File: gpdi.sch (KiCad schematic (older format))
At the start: 20 parts, among them U1 LFE5U-45F-6BG381C, U11 PCA9306D

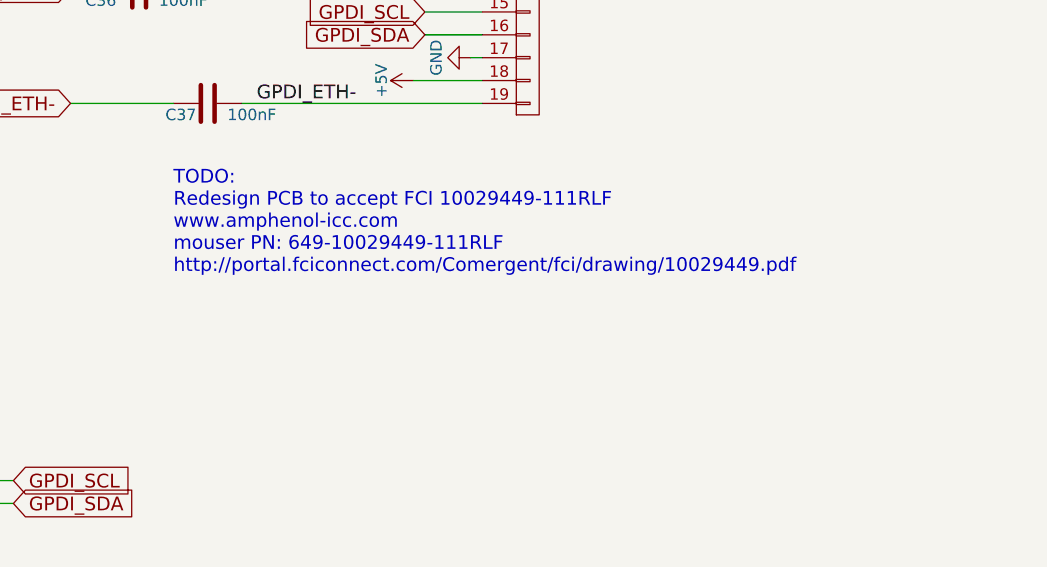
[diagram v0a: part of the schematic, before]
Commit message: schematics: GPDI1 connector part number set to FCI 10029449-111RLF
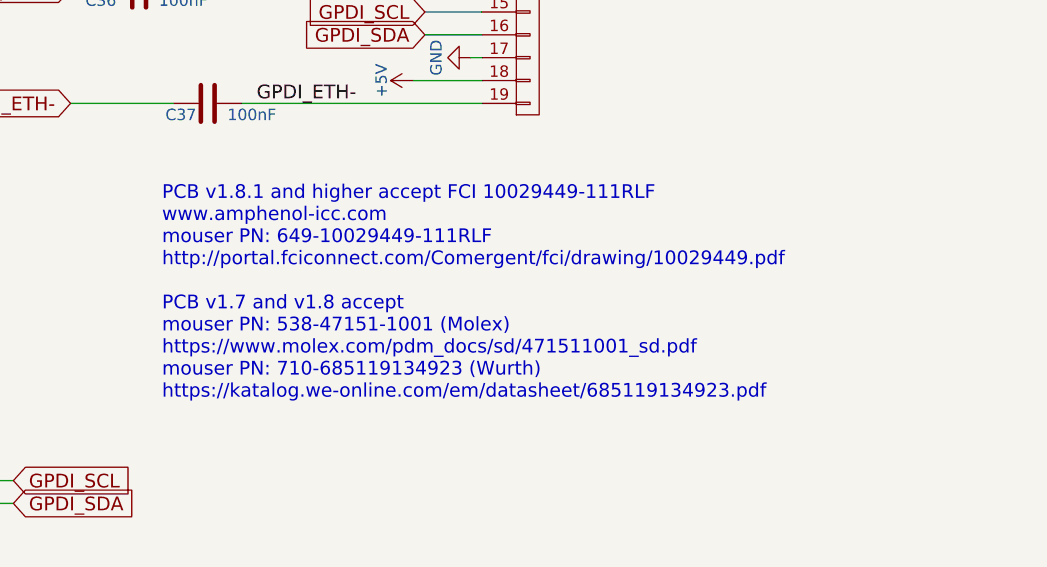
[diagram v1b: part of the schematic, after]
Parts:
- GPDI1: Distributor1_PN 710-685119134923 -> 649-10029449-111RLF; Distributor2_PN: 538-47151-1001 -> (none); Distributor2_URL www.mouser.com -> (none); MFG2_PN 47151-1001 -> (none); MFG2_URL www.molex.com -> (none); MFG_PN 685119134923 -> 10029449-111RLF; MFG_URL www.we-online.com -> www.amphenol-icc.com
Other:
- note added: "PCB v1.8.1 and higher accept FCI 10029449-111RLF\nwww.amphenol-icc.com\nmouser PN: 649-10029449-111RLF\nhttp://portal.fciconnect.com/Comergent/fci/drawing/10029449.pdf\n\nPCB v1.7 and v1.8 accept\nmouser PN: 538-47151-1001 (Molex)\nhttps://www.molex.com/pdm_docs/sd/471511001_sd.pdf\nmouser PN: 710-685119134923 (Wurth)\nhttps://katalog.we-online.com/em/datasheet/685119134923.pdf"
- note removed: "TODO:\nRedesign PCB to accept FCI 10029449-111RLF\nwww.amphenol-icc.com\nmouser PN: 649-10029449-111RLF\nhttp://portal.fciconnect.com/Comergent/fci/drawing/10029449.pdf\n"
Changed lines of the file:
@@
 F 1 "GPDI-D" V 9050 2950 50  0000 C CNN
 F 2 "conn-fci:CONN-10029449-111RLF" H 8950 2950 60  0001 C CNN
-F 3 "https://katalog.we-online.com/em/datasheet/685119134923.pdf" H 8950 2950 60  0001 C CNN
-F 4 "www.we-online.com" H 8950 2950 60  0001 C CNN "MFG_URL"
-F 5 "685119134923" H 8950 2950 60  0001 C CNN "MFG_PN"
-F 6 "www.molex.com" H 8950 2950 50  0001 C CNN "MFG2_URL"
-F 7 "47151-1001" H 8950 2950 50  0001 C CNN "MFG2_PN"
-F 8 "www.mouser.com" H 8950 2950 60  0001 C CNN "Distributor1_URL"
-F 9 "710-685119134923" H 8950 2950 60  0001 C CNN "Distributor1_PN"
-F 10 "www.mouser.com" H 8950 2950 50  0001 C CNN "Distributor2_URL"
-F 11 "538-47151-1001" H 8950 2950 50  0001 C CNN "Distributor2_PN:"
+F 3 "http://portal.fciconnect.com/Comergent/fci/drawing/10029449.pdf" H 8950 2950 60  0001 C CNN
+F 4 "www.amphenol-icc.com" H 8950 2950 60  0001 C CNN "MFG_URL"
+F 5 "10029449-111RLF" H 8950 2950 60  0001 C CNN "MFG_PN"
+F 6 "www.mouser.com" H 8950 2950 60  0001 C CNN "Distributor1_URL"
+F 7 "649-10029449-111RLF" H 8950 2950 60  0001 C CNN "Distributor1_PN"
 	1    8950 2950
 	1    0    0    -1
@@
 Wire Wire Line
 	6100 5450 6100 5750
-Text Notes 7400 4650 0    60   ~ 0
-TODO:\nRedesign PCB to accept FCI 10029449-111RLF\nwww.amphenol-icc.com\nmouser PN: 649-10029449-111RLF\nhttp://portal.fciconnect.com/Comergent/fci/drawing/10029449.pdf\n
+Text Notes 7350 5200 0    60   ~ 0
+PCB v1.8.1 and higher accept FCI 10029449-111RLF\nwww.amphenol-icc.com\nmouser PN: 649-10029449-111RLF\nhttp://portal.fciconnect.com/Comergent/fci/drawing/10029449.pdf\n\nPCB v1.7 and v1.8 accept\nmouser PN: 538-47151-1001 (Molex)\nhttps://www.molex.com/pdm_docs/sd/471511001_sd.pdf\nmouser PN: 710-685119134923 (Wurth)\nhttps://katalog.we-online.com/em/datasheet/685119134923.pdf
 $EndSCHEMATC

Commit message: schematics: replace 45F chip with 85F
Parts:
- U1: value LFE5U-45F-6BG381C -> LFE5U-85F-6BG381C; symbol lfe5bg381:LFE5U-45F-6BG381C -> lfe5bg381:LFE5U-85F-6BG381C; MFG_PN LFE5U-45F-6BG381C -> LFE5U-85F-6BG381C
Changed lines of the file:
@@
 	6100 4850 6300 4850
 $Comp
-L lfe5bg381:LFE5U-45F-6BG381C U1
+L lfe5bg381:LFE5U-85F-6BG381C U1
 U 2 1 5A07A906
 P 3600 2900
@@
 AR Path="/58D686D9/5A07A906" Ref="U1"  Part="2"
 F 0 "U1" H 3600 3850 60  0000 C CNN
-F 1 "LFE5U-45F-6BG381C" H 3600 3750 60  0000 C CNN
+F 1 "LFE5U-85F-6BG381C" H 3600 3750 60  0000 C CNN
 F 2 "lfe5bg381:BGA-381_pitch0.8mm_dia0.4mm" H 2550 3850 60  0001 C CNN
 F 3 "http://www.latticesemi.com/~/media/LatticeSemi/Documents/DataSheets/ECP5/FPGA-DS-02012.pdf" H 2550 3850 60  0001 C CNN
-F 4 "LFE5U-45F-6BG381C" H 3600 2900 60  0001 C CNN "MFG_PN"
+F 4 "LFE5U-85F-6BG381C" H 3600 2900 60  0001 C CNN "MFG_PN"
 F 5 "www.mouser.com" H 3600 2900 60  0001 C CNN "Distributor1_URL"
 	2    3600 2900

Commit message: schematics: instead of micro-gpdi-d symbol using gpdi-d
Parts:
- GPDI1: symbol micro-hdmi-d:MICRO-HDMI-D -> hdmi-d:HDMI-D
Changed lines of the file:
@@
 $EndDescr
 $Comp
-L micro-hdmi-d:MICRO-HDMI-D GPDI1
+L hdmi-d:HDMI-D GPDI1
 U 1 1 58D69067
 P 8950 2950

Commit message: schematics: hopefully getting rid of all references to micro-gpdi-d
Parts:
- U11: symbol micro-hdmi-d:DIL8 -> Connector_Generic:Conn_02x04_Counter_Clockwise
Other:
- moved on the sheet: R22, R23
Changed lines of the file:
@@
 GPDI_SDA
 $Comp
-L micro-hdmi-d:DIL8 U11
+L Connector_Generic:Conn_02x04_Counter_Clockwise U11
 U 1 1 58D91A1E
-P 5300 5500
-F 0 "U11" H 5300 5750 50  0000 C CNN
-F 1 "PCA9306D" H 5300 5250 50  0000 C CNN
-F 2 "SM8:SM8" H 5300 5500 50  0001 C CNN
-F 3 "https://www.nxp.com/docs/en/data-sheet/PCA9306.pdf" H 5300 5500 50  0001 C CNN
-F 4 "www.nxp.com" H 5300 5500 60  0001 C CNN "MFG_URL"
-F 5 "PCA9306D" H 5300 5500 60  0001 C CNN "MFG_PN"
-F 6 "www.mouser.com" H 5300 5500 60  0001 C CNN "Distributor1_URL"
-F 7 "771-PCA9306D-T" H 5300 5500 60  0001 C CNN "Distributor1_PN"
-	1    5300 5500
+P 5350 5450
+F 0 "U11" H 5400 5650 50  0000 C CNN
+F 1 "PCA9306D" H 5400 5150 50  0000 C CNN
+F 2 "SM8:SM8" H 5350 5450 50  0001 C CNN
+F 3 "https://www.nxp.com/docs/en/data-sheet/PCA9306.pdf" H 5350 5450 50  0001 C CNN
+F 4 "www.nxp.com" H 5350 5450 60  0001 C CNN "MFG_URL"
+F 5 "PCA9306D" H 5350 5450 60  0001 C CNN "MFG_PN"
+F 6 "www.mouser.com" H 5350 5450 60  0001 C CNN "Distributor1_URL"
+F 7 "771-PCA9306D-T" H 5350 5450 60  0001 C CNN "Distributor1_PN"
+	1    5350 5450
 	1    0    0    -1
 $EndComp
@@
 L power:+3V3 #PWR091
 U 1 1 58D92A40
-P 4700 5000
-F 0 "#PWR091" H 4700 4850 50  0001 C CNN
-F 1 "+3V3" H 4700 5140 50  0000 C CNN
-F 2 "" H 4700 5000 50  0000 C CNN
-F 3 "" H 4700 5000 50  0000 C CNN
-	1    4700 5000
+P 4900 5000
+F 0 "#PWR091" H 4900 4850 50  0001 C CNN
+F 1 "+3V3" H 4900 5140 50  0000 C CNN
+F 2 "" H 4900 5000 50  0000 C CNN
+F 3 "" H 4900 5000 50  0000 C CNN
+	1    4900 5000
 	1    0    0    -1
 $EndComp
@@
 L power:GND #PWR092
 U 1 1 58D92B02
-P 4950 5350
-F 0 "#PWR092" H 4950 5100 50  0001 C CNN
-F 1 "GND" H 4950 5200 50  0000 C CNN
-F 2 "" H 4950 5350 50  0000 C CNN
-F 3 "" H 4950 5350 50  0000 C CNN
-	1    4950 5350
+P 5150 5350
+F 0 "#PWR092" H 5150 5100 50  0001 C CNN
+F 1 "GND" H 5150 5200 50  0000 C CNN
+F 2 "" H 5150 5350 50  0000 C CNN
+F 3 "" H 5150 5350 50  0000 C CNN
+	1    5150 5350
 	0    1    1    0
 $EndComp
@@
 L ulx3s-rescue:R R23
 U 1 1 58D92CF9
-P 4400 5300
-F 0 "R23" V 4480 5300 50  0000 C CNN
-F 1 "2.2k" V 4400 5300 50  0000 C CNN
-F 2 "Resistors_SMD:R_0603_HandSoldering" V 4330 5300 50  0001 C CNN
-F 3 "" H 4400 5300 50  0000 C CNN
-	1    4400 5300
+P 4600 5300
+F 0 "R23" V 4680 5300 50  0000 C CNN
+F 1 "2.2k" V 4600 5300 50  0000 C CNN
+F 2 "Resistors_SMD:R_0603_HandSoldering" V 4530 5300 50  0001 C CNN
+F 3 "" H 4600 5300 50  0000 C CNN
+	1    4600 5300
 	1    0    0    -1
 $EndComp
@@
 L ulx3s-rescue:R R22
 U 1 1 58D92D93
-P 4250 5300
-F 0 "R22" V 4330 5300 50  0000 C CNN
-F 1 "2.2k" V 4250 5300 50  0000 C CNN
-F 2 "Resistors_SMD:R_0603_HandSoldering" V 4180 5300 50  0001 C CNN
-F 3 "" H 4250 5300 50  0000 C CNN
-	1    4250 5300
+P 4450 5300
+F 0 "R22" V 4530 5300 50  0000 C CNN
+F 1 "2.2k" V 4450 5300 50  0000 C CNN
+F 2 "Resistors_SMD:R_0603_HandSoldering" V 4380 5300 50  0001 C CNN
+F 3 "" H 4450 5300 50  0000 C CNN
+	1    4450 5300
 	1    0    0    -1
 $EndComp
@@
 Text GLabel 6700 5550 2    60   Input ~ 0
 GPDI_SCL
-Text GLabel 4100 5550 0    60   Input ~ 0
+Text GLabel 4300 5550 0    60   Input ~ 0
 FPDI_SCL
-Text GLabel 4100 5650 0    60   Input ~ 0
+Text GLabel 4300 5650 0    60   Input ~ 0
 FPDI_SDA
 Text Label 5700 5450 0    60   ~ 0
@@
 	8750 2000 8700 2000
 Wire Wire Line
-	4700 5450 4950 5450
-Wire Wire Line
-	4100 5550 4400 5550
-Wire Wire Line
-	4100 5650 4250 5650
+	4900 5450 5150 5450
+Wire Wire Line
+	4300 5550 4600 5550
+Wire Wire Line
+	4300 5650 4450 5650
 Wire Wire Line
 	5650 5350 6100 5350
@@
 	6100 6050 6100 6100
 Wire Wire Line
-	4700 5000 4700 5050
-Wire Wire Line
-	4400 5550 4400 5450
-Wire Wire Line
-	4250 5650 4250 5450
-Wire Wire Line
-	4250 5150 4250 5050
-Wire Wire Line
-	4250 5050 4400 5050
-Connection ~ 4700 5050
-Wire Wire Line
-	4400 5050 4400 5150
-Connection ~ 4400 5050
+	4900 5000 4900 5050
+Wire Wire Line
+	4600 5550 4600 5450
+Wire Wire Line
+	4450 5650 4450 5450
+Wire Wire Line
+	4450 5150 4450 5050
+Wire Wire Line
+	4450 5050 4600 5050
+Connection ~ 4900 5050
+Wire Wire Line
+	4600 5050 4600 5150
+Connection ~ 4600 5050
 Connection ~ 6300 5550
 Connection ~ 6500 5650
-Connection ~ 4400 5550
-Connection ~ 4250 5650
+Connection ~ 4600 5550
+Connection ~ 4450 5650
 Connection ~ 6100 5450
 Wire Wire Line
@@
 Text Label 1800 2300 0    60   ~ 0
 FPDI_CEC
-Text Notes 3500 5950 0    60   ~ 0
+Text Notes 3700 5950 0    60   ~ 0
 i2c shared with RTC\non "power" sheet
 Text Notes 1600 2850 0    60   ~ 0
@@
 	6300 4850 6500 4850
 Wire Wire Line
-	4700 5050 4700 5450
-Wire Wire Line
-	4400 5050 4700 5050
+	4900 5050 4900 5450
+Wire Wire Line
+	4600 5050 4900 5050
 Wire Wire Line
 	6300 5550 6700 5550
@@
 	6500 5650 6700 5650
 Wire Wire Line
-	4400 5550 4950 5550
-Wire Wire Line
-	4250 5650 4950 5650
+	4600 5550 5150 5550
+Wire Wire Line
+	4450 5650 5150 5650
 Wire Wire Line
 	6100 5450 6100 5750

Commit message: schematics: updating resistor footprints
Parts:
- R22, R23, R24, R25, R26: footprint Resistors_SMD:R_0603_HandSoldering -> Resistor_SMD:R_0603_1608Metric_Pad0.84x1.00mm_HandSolder
- R61: footprint Resistors_SMD:R_0603_HandSoldering -> Resistor_SMD:R_0603_1608Metric
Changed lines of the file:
@@
 F 0 "R24" V 6180 5100 50  0000 C CNN
 F 1 "100k" V 6100 5100 50  0000 C CNN
-F 2 "Resistors_SMD:R_0603_HandSoldering" V 6030 5100 50  0001 C CNN
+F 2 "Resistor_SMD:R_0603_1608Metric_Pad0.84x1.00mm_HandSolder" V 6030 5100 50  0001 C CNN
 F 3 "" H 6100 5100 50  0000 C CNN
 	1    6100 5100
@@
 F 0 "R25" V 6380 5100 50  0000 C CNN
 F 1 "4.7k" V 6300 5100 50  0000 C CNN
-F 2 "Resistors_SMD:R_0603_HandSoldering" V 6230 5100 50  0001 C CNN
+F 2 "Resistor_SMD:R_0603_1608Metric_Pad0.84x1.00mm_HandSolder" V 6230 5100 50  0001 C CNN
 F 3 "" H 6300 5100 50  0000 C CNN
 	1    6300 5100
@@
 F 0 "R26" V 6580 5100 50  0000 C CNN
 F 1 "4.7k" V 6500 5100 50  0000 C CNN
-F 2 "Resistors_SMD:R_0603_HandSoldering" V 6430 5100 50  0001 C CNN
+F 2 "Resistor_SMD:R_0603_1608Metric_Pad0.84x1.00mm_HandSolder" V 6430 5100 50  0001 C CNN
 F 3 "" H 6500 5100 50  0000 C CNN
 	1    6500 5100
@@
 F 0 "R23" V 4680 5300 50  0000 C CNN
 F 1 "2.2k" V 4600 5300 50  0000 C CNN
-F 2 "Resistors_SMD:R_0603_HandSoldering" V 4530 5300 50  0001 C CNN
+F 2 "Resistor_SMD:R_0603_1608Metric_Pad0.84x1.00mm_HandSolder" V 4530 5300 50  0001 C CNN
 F 3 "" H 4600 5300 50  0000 C CNN
 	1    4600 5300
@@
 F 0 "R22" V 4530 5300 50  0000 C CNN
 F 1 "2.2k" V 4450 5300 50  0000 C CNN
-F 2 "Resistors_SMD:R_0603_HandSoldering" V 4380 5300 50  0001 C CNN
+F 2 "Resistor_SMD:R_0603_1608Metric_Pad0.84x1.00mm_HandSolder" V 4380 5300 50  0001 C CNN
 F 3 "" H 4450 5300 50  0000 C CNN
 	1    4450 5300
@@
 F 0 "R61" V 1680 2300 50  0000 C CNN
 F 1 "470" V 1600 2300 50  0000 C CNN
-F 2 "Resistors_SMD:R_0603_HandSoldering" V 1530 2300 50  0001 C CNN
+F 2 "Resistor_SMD:R_0603_1608Metric" V 1530 2300 50  0001 C CNN
 F 3 "" H 1600 2300 50  0000 C CNN
 	1    1600 2300

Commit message: schematics: alternate GPDI1 distributor part number
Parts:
- GPDI1: Datasheet2 (none) -> https://hr.mouser.com/datasheet/2/418/NG_CD_1903015_S-66266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; Distributor2_PN (none) -> 571-5-1903015-5; Distributor2_URL (none) -> www.mouser.com
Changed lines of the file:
@@
 F 6 "www.mouser.com" H 8950 2950 60  0001 C CNN "Distributor1_URL"
 F 7 "649-10029449-111RLF" H 8950 2950 60  0001 C CNN "Distributor1_PN"
+F 8 "www.mouser.com" H 8950 2950 50  0001 C CNN "Distributor2_URL"
+F 9 "571-5-1903015-5" H 8950 2950 50  0001 C CNN "Distributor2_PN"
+F 10 "https://hr.mouser.com/datasheet/2/418/NG_CD_1903015_S-662666.pdf" H 8950 2950 50  0001 C CNN "Datasheet2"
 	1    8950 2950
 	1    0    0    -1

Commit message: schematics: set part numbers for most resistors
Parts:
- R22, R23: MFG_PN (none) -> RC0603FR-072K2L
- R24: MFG_PN (none) -> AC0603FR-10100KL
- R25, R26: MFG_PN (none) -> AC0603FR-104K7L
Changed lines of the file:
@@
 F 2 "Resistor_SMD:R_0603_1608Metric_Pad0.84x1.00mm_HandSolder" V 6030 5100 50  0001 C CNN
 F 3 "" H 6100 5100 50  0000 C CNN
+F 4 "AC0603FR-10100KL" V 6100 5100 50  0001 C CNN "MFG_PN"
 	1    6100 5100
 	1    0    0    -1
@@
 F 2 "Resistor_SMD:R_0603_1608Metric_Pad0.84x1.00mm_HandSolder" V 6230 5100 50  0001 C CNN
 F 3 "" H 6300 5100 50  0000 C CNN
+F 4 "AC0603FR-104K7L" V 6300 5100 50  0001 C CNN "MFG_PN"
 	1    6300 5100
 	1    0    0    -1
@@
 F 2 "Resistor_SMD:R_0603_1608Metric_Pad0.84x1.00mm_HandSolder" V 6430 5100 50  0001 C CNN
 F 3 "" H 6500 5100 50  0000 C CNN
+F 4 "AC0603FR-104K7L" V 6500 5100 50  0001 C CNN "MFG_PN"
 	1    6500 5100
 	1    0    0    -1
@@
 F 2 "Resistor_SMD:R_0603_1608Metric_Pad0.84x1.00mm_HandSolder" V 4530 5300 50  0001 C CNN
 F 3 "" H 4600 5300 50  0000 C CNN
+F 4 "RC0603FR-072K2L" V 4600 5300 50  0001 C CNN "MFG_PN"
 	1    4600 5300
 	1    0    0    -1
@@
 F 2 "Resistor_SMD:R_0603_1608Metric_Pad0.84x1.00mm_HandSolder" V 4380 5300 50  0001 C CNN
 F 3 "" H 4450 5300 50  0000 C CNN
+F 4 "RC0603FR-072K2L" V 4450 5300 50  0001 C CNN "MFG_PN"
 	1    4450 5300
 	1    0    0    -1

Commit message: schematics: updating R,C part numbers
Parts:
- C18: MFG_PN (none) -> CS0603KRX7R9BB471
- C36, C37, C38, C39, C40, C41, C42, C43, C44, C45: MFG_PN (none) -> CC0603KRX7R8BB104
- R61: MFG_PN (none) -> RC0603FR-07470RL
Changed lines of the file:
@@
 F 2 "Capacitor_SMD:C_0603_1608Metric" H 6138 5750 50  0001 C CNN
 F 3 "" H 6100 5900 50  0000 C CNN
+F 4 "CS0603KRX7R9BB471" H 6100 5900 50  0001 C CNN "MFG_PN"
 	1    6100 5900
 	1    0    0    -1
@@
 F 2 "Resistor_SMD:R_0603_1608Metric" V 1530 2300 50  0001 C CNN
 F 3 "" H 1600 2300 50  0000 C CNN
+F 4 "RC0603FR-07470RL" V 1600 2300 50  0001 C CNN "MFG_PN"
 	1    1600 2300
 	0    -1   -1   0
@@
 F 2 "Capacitor_SMD:C_0603_1608Metric" H 7288 3250 50  0001 C CNN
 F 3 "" H 7250 3400 50  0000 C CNN
+F 4 "CC0603KRX7R8BB104" V 7250 3400 50  0001 C CNN "MFG_PN"
 	1    7250 3400
 	0    -1   1    0
@@
 F 2 "Capacitor_SMD:C_0603_1608Metric" H 7588 3750 50  0001 C CNN
 F 3 "" H 7550 3900 50  0000 C CNN
+F 4 "CC0603KRX7R8BB104" V 7550 3900 50  0001 C CNN "MFG_PN"
 	1    7550 3900
 	0    -1   1    0
@@
 F 2 "Capacitor_SMD:C_0603_1608Metric" H 7288 2850 50  0001 C CNN
 F 3 "" H 7250 3000 50  0000 C CNN
+F 4 "CC0603KRX7R8BB104" V 7250 3000 50  0001 C CNN "MFG_PN"
 	1    7250 3000
 	0    -1   1    0
@@
 F 2 "Capacitor_SMD:C_0603_1608Metric" H 7588 3050 50  0001 C CNN
 F 3 "" H 7550 3200 50  0000 C CNN
+F 4 "CC0603KRX7R8BB104" V 7550 3200 50  0001 C CNN "MFG_PN"
 	1    7550 3200
 	0    -1   1    0
@@
 F 2 "Capacitor_SMD:C_0603_1608Metric" H 7588 2750 50  0001 C CNN
 F 3 "" H 7550 2900 50  0000 C CNN
+F 4 "CC0603KRX7R8BB104" V 7550 2900 50  0001 C CNN "MFG_PN"
 	1    7550 2900
 	0    -1   1    0
@@
 F 2 "Capacitor_SMD:C_0603_1608Metric" H 7288 2550 50  0001 C CNN
 F 3 "" H 7250 2700 50  0000 C CNN
+F 4 "CC0603KRX7R8BB104" V 7250 2700 50  0001 C CNN "MFG_PN"
 	1    7250 2700
 	0    -1   1    0
@@
 F 2 "Capacitor_SMD:C_0603_1608Metric" H 7588 2450 50  0001 C CNN
 F 3 "" H 7550 2600 50  0000 C CNN
+F 4 "CC0603KRX7R8BB104" V 7550 2600 50  0001 C CNN "MFG_PN"
 	1    7550 2600
 	0    -1   1    0
@@
 F 2 "Capacitor_SMD:C_0603_1608Metric" H 7288 2250 50  0001 C CNN
 F 3 "" H 7250 2400 50  0000 C CNN
+F 4 "CC0603KRX7R8BB104" V 7250 2400 50  0001 C CNN "MFG_PN"
 	1    7250 2400
 	0    -1   1    0
@@
 F 2 "Capacitor_SMD:C_0603_1608Metric" H 7288 1950 50  0001 C CNN
 F 3 "" H 7250 2100 50  0000 C CNN
+F 4 "CC0603KRX7R8BB104" V 7250 2100 50  0001 C CNN "MFG_PN"
 	1    7250 2100
 	0    -1   1    0
@@
 F 2 "Capacitor_SMD:C_0603_1608Metric" H 7588 2150 50  0001 C CNN
 F 3 "" H 7550 2300 50  0000 C CNN
+F 4 "CC0603KRX7R8BB104" V 7550 2300 50  0001 C CNN "MFG_PN"
 	1    7550 2300
 	0    -1   1    0
